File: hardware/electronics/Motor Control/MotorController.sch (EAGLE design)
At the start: 10 parts, among them J1 AVR_SPI_PRG_6PTH, U1 ARDUINOR3-BPLACE, U2 ATMEGA328P_TQFP, U3 V_REG_317SMD, X1 HEADER_POS3_70555

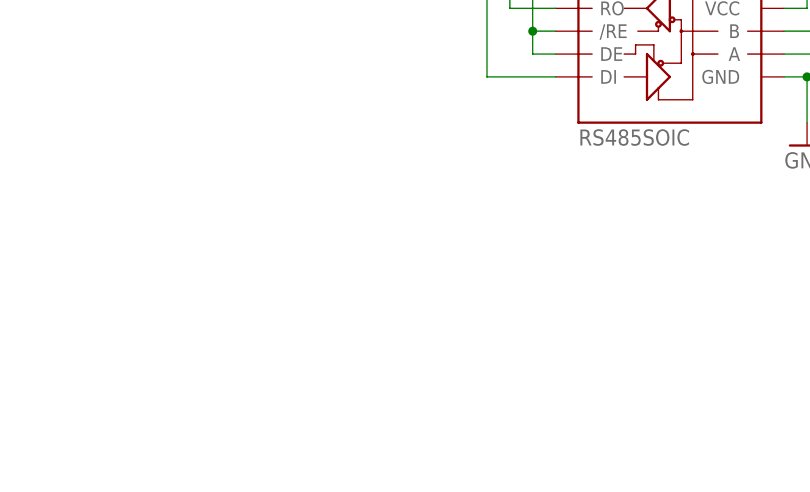
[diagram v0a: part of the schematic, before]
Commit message: Making sure we have the latest board in github
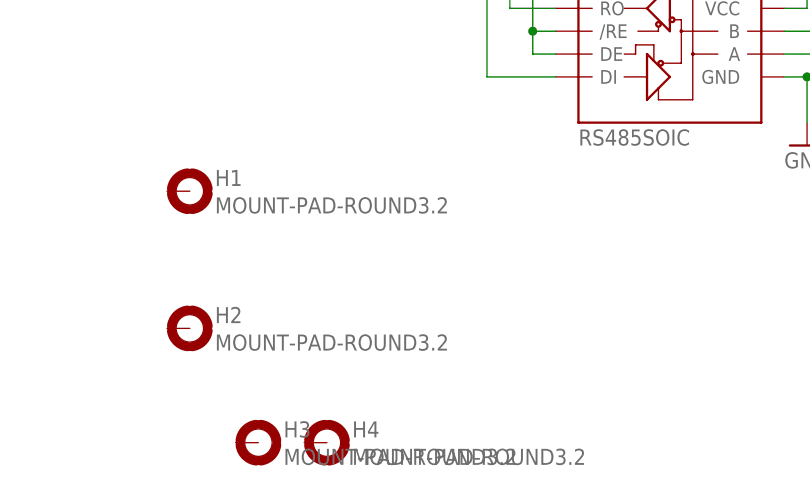
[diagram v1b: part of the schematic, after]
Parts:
- added H1, H2, H3, H4: MOUNT-PAD-ROUND3.2, holes:MOUNT-PAD-ROUND3.2
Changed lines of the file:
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@@
 <part name="C4" library="resistor" deviceset="C-EU" device="C1206"/>
 <part name="X1" library="con-molex-c-grid-sl" deviceset="HEADER_POS3_?" device="70555"/>
+<part name="H1" library="holes" deviceset="MOUNT-PAD-ROUND" device="3.2"/>
+<part name="H2" library="holes" deviceset="MOUNT-PAD-ROUND" device="3.2"/>
+<part name="H3" library="holes" deviceset="MOUNT-PAD-ROUND" device="3.2"/>
+<part name="H4" library="holes" deviceset="MOUNT-PAD-ROUND" device="3.2"/>
 </parts>
 <sheets>
@@
 <instance part="C4" gate="G$1" x="193.04" y="93.98" rot="R180"/>
 <instance part="X1" gate="G$1" x="154.94" y="76.2"/>
+<instance part="H1" gate="G$1" x="60.96" y="60.96"/>
+<instance part="H2" gate="G$1" x="60.96" y="45.72"/>
+<instance part="H3" gate="G$1" x="68.58" y="33.02"/>
+<instance part="H4" gate="G$1" x="76.2" y="33.02"/>
 </instances>
 <busses>
